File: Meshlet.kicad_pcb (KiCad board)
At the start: 4 copper layers, 42.5 x 32 mm, 101 parts, among them J12 GPS Header, J13 Thermistor Pins, J14 Ext. Notif. Header, J2 User Btn Header, J3 Batt. Header (Picoblade 1.25), J4 Batt. Header (JST-PH 2.0), J5 USB_C_Receptacle_USB2.0_16P, J6 I2C Header, J7 Ext. Power Header, J9 Ext. Power Header, Q1 AO3400A, SW2 BOOTSEL, U1 XC6206PxxxMR, U11 INA3221, U2 USBLC6-2SC6, U3 XC6206PxxxMR, U4 RP2350_60QFN, U5 Wio-SX1262, U6 BQ25185, U7 BME280, U8 W25Q32JVZP, U9 XC6206PxxxMR, Y1 12.000MHz

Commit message: Trace and zone tune-ups
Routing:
- net GND: track 3.42 -> 5.47 mm, vias 316 -> 275
- net /Pi +3V3: track 102.7 -> 103.3 mm
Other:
- board text added: "SOLAR/EXT 3.3V-18V"
- board text removed: "EXT. INPUT 3.3V-18V"

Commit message: Rounded all of the traces on the top layer. For fun
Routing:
- net /LoRa +3V3: track 49.0 -> 50.8 mm
- net USER_BTN: track 13.1 -> 14.4 mm
- net +3V3: track 89.7 -> 88.6 mm
- net Net-(U6-STAT2): track 9.58 -> 10.5 mm
- net /Pi +3V3: track 103.3 -> 104.2 mm
- net NOTIFY: track 15.8 -> 16.6 mm
- net LORA_IRQ: track 14.2 -> 14.8 mm
- net HB: track 27.8 -> 28.4 mm
- net VSET: track 9.04 -> 9.59 mm
- net GND: track 5.47 -> 5.48 mm, vias 275 -> 262

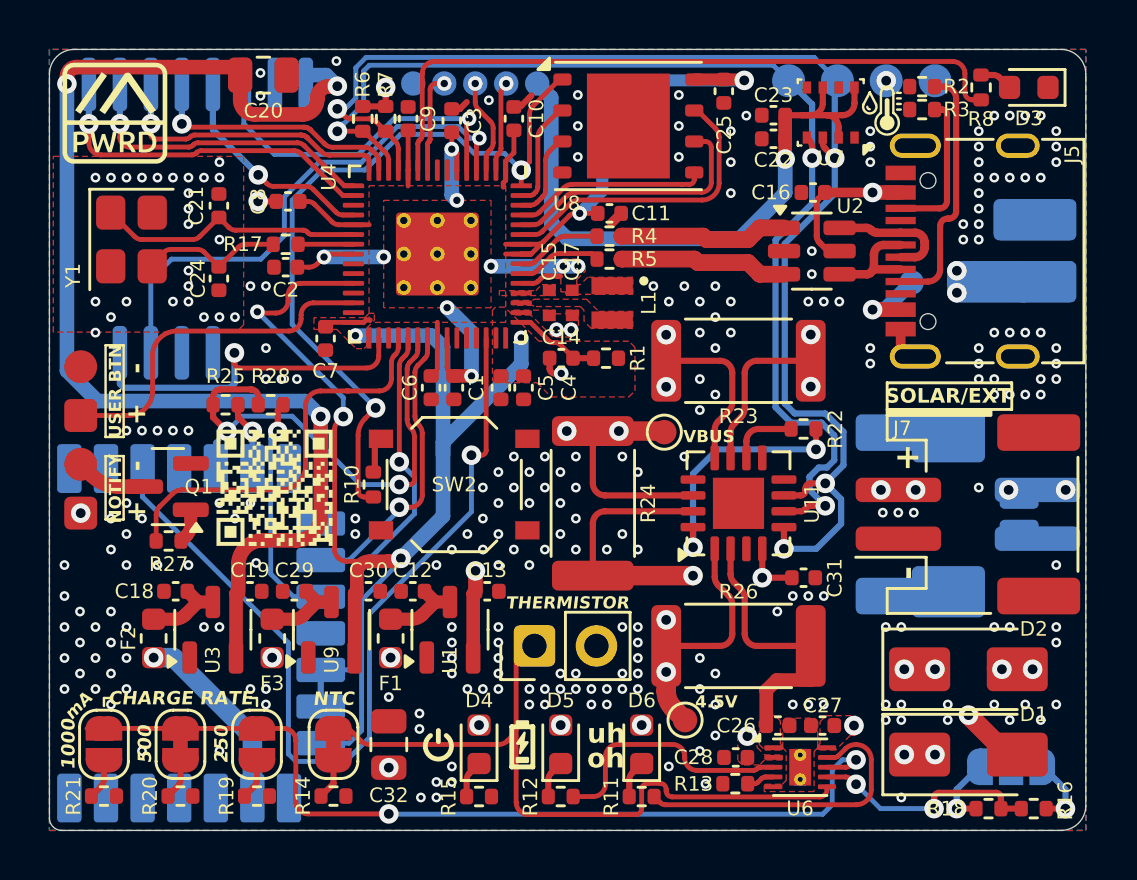
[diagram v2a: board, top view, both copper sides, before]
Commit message: Rounded traces on the back side too, updated ibom
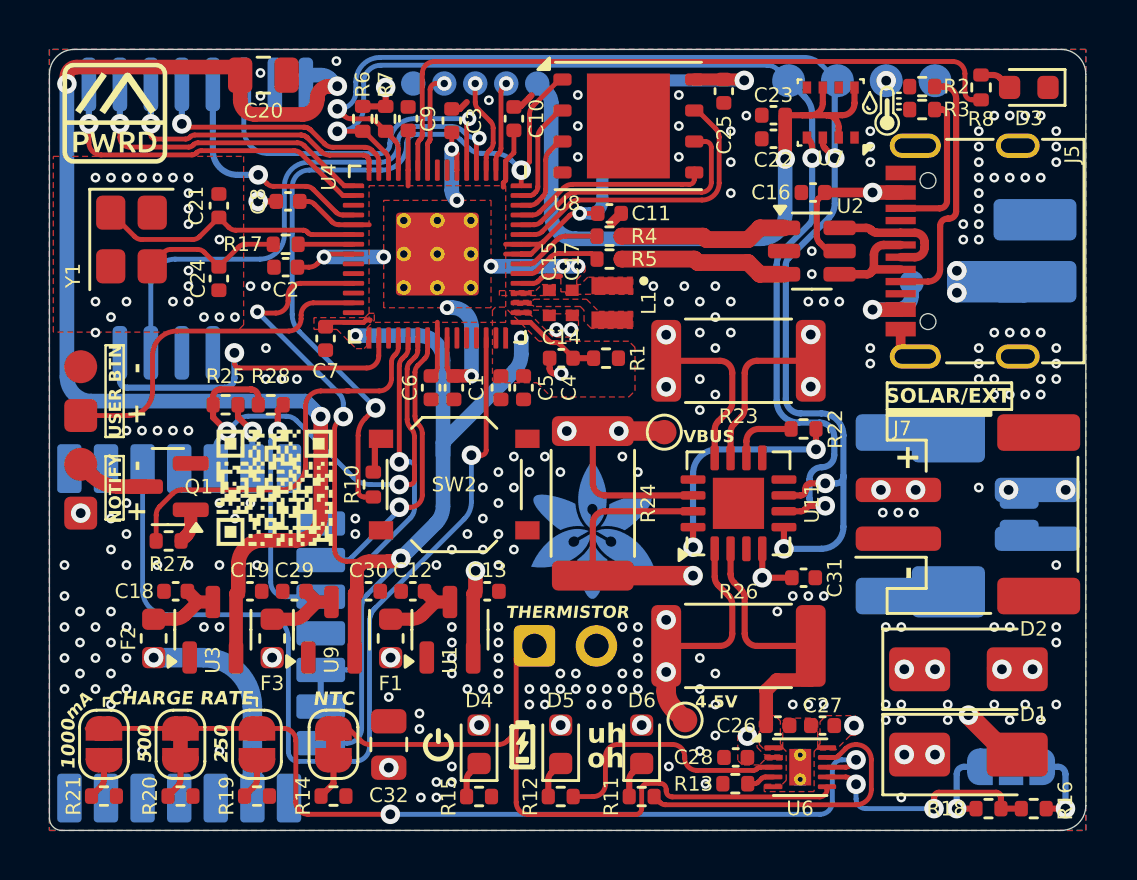
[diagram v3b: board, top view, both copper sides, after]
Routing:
- net GP29: track 36.6 -> 39.4 mm
- net BMS_OUT: track 48.0 -> 48.9 mm
- net LORA_RST: track 9.02 -> 9.64 mm
- net LORA_BUSY: track 21.5 -> 22.2 mm
- net +3V3: track 88.6 -> 89.1 mm
- net GND: vias 262 -> 242
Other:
- board text added: "by dj505"
- board text added: "designed in Edmonton, AB"
- board text added: "rev 1.0"
- board text removed: "DESIGNED IN EDMONTON, AB"

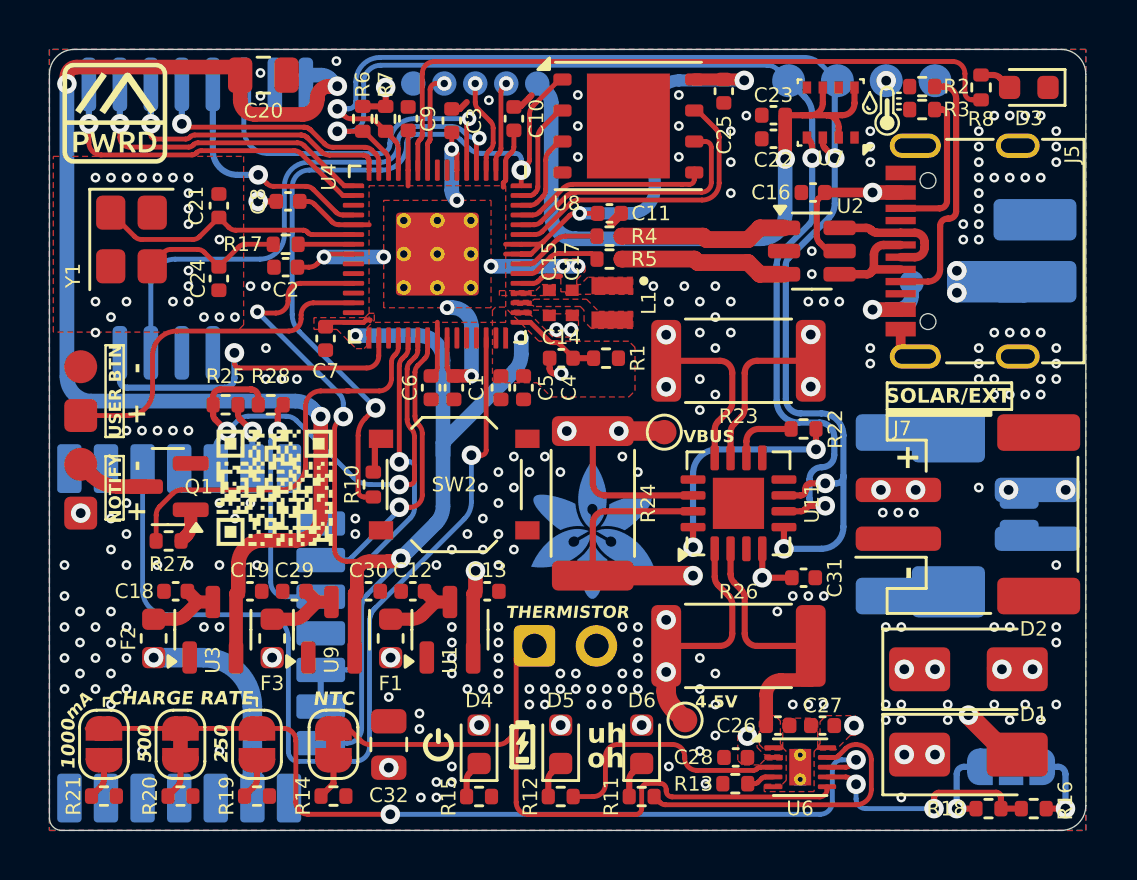
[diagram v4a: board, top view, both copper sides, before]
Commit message: Bigger vias. Less manufacturing fees. I hope
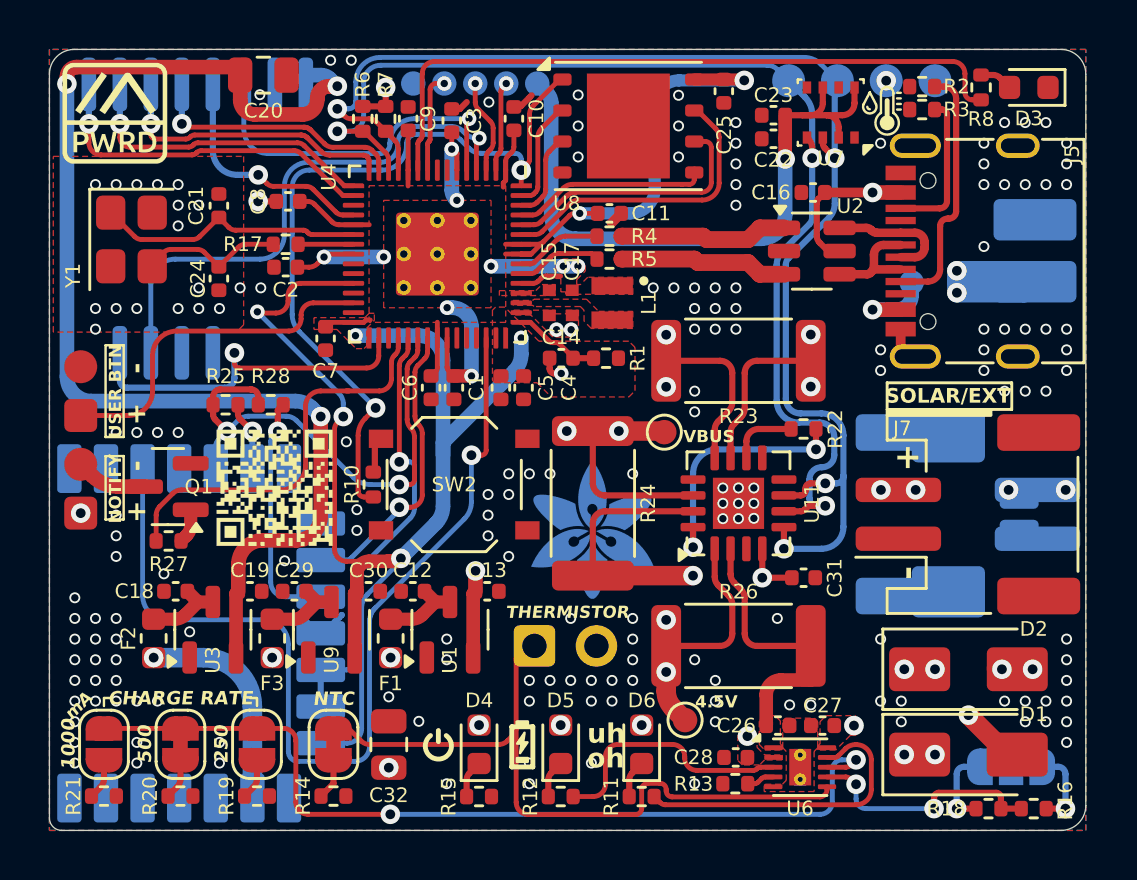
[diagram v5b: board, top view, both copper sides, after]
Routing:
- net GND: track 5.48 -> 8.08 mm, vias 242 -> 178
- net ISET: track 37.7 -> 37.0 mm

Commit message: accidentally shorted the inner layers oops
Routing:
- net +3V3: track 89.1 -> 90.3 mm
- net VBUS_OUT: track 28.8 -> 29.4 mm
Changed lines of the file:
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@@
-	(segment
-		(start 152.6289 83.028)
-		(end 151.384 84.2729)
-		(width 0.8)
-		(layer "In1.Cu")
-		(net 4)
-	)
 	(segment
 		(start 152.6289 83.028)
@@
 	)
 	(segment
-		(start 151.384 99.879799)
-		(end 151.6902 100.185999)
-		(width 0.8)
-		(layer "In1.Cu")
-		(net 4)
-	)
-	(segment
 		(start 154.0129 79.8195)
 		(end 156.7688 79.8195)
@@
 	)
 	(segment
-		(start 151.384 84.2729)
-		(end 151.384 99.879799)
+		(start 153.5303 99.5553)
+		(end 152.899601 100.185999)
+		(width 0.8)
+		(layer "In1.Cu")
+		(net 4)
+	)
+	(segment
+		(start 152.6286 83.0283)
+		(end 152.6286 97.4344)
+		(width 0.8)
+		(layer "In1.Cu")
+		(net 4)
+	)
+	(segment
+		(start 152.6289 83.028)
+		(end 152.6286 83.0283)
+		(width 0.8)
+		(layer "In1.Cu")
+		(net 4)
+	)
+	(segment
+		(start 152.6286 97.4344)
+		(end 153.5303 98.3361)
+		(width 0.8)
+		(layer "In1.Cu")
+		(net 4)
+	)
+	(segment
+		(start 152.899601 100.185999)
+		(end 151.6902 100.185999)
+		(width 0.8)
+		(layer "In1.Cu")
+		(net 4)
+	)
+	(segment
+		(start 153.5303 98.3361)
+		(end 153.5303 99.5553)
 		(width 0.8)
 		(layer "In1.Cu")
@@
 	)
 	(segment
+		(start 151.7819 95.2796)
+		(end 152.71965 96.21735)
+		(width 0.8)
+		(layer "In2.Cu")
+		(net 11)
+	)
+	(segment
 		(start 145.813 94.1755)
 		(end 149.5645 94.1755)
@@
 	(segment
 		(start 149.5645 94.1755)
+		(end 150.6686 95.2796)
+		(width 0.8)
+		(layer "In2.Cu")
+		(net 11)
+	)
+	(segment
+		(start 155.4468 100.0578)
+		(end 155.4468 106.243599)
+		(width 0.8)
+		(layer "In2.Cu")
+		(net 11)
+	)
+	(segment
+		(start 152.71965 97.33065)
 		(end 155.4468 100.0578)
 		(width 0.8)
@@
 	)
 	(segment
-		(start 155.4468 100.0578)
-		(end 155.4468 106.243599)
-		(width 0.8)
-		(layer "In2.Cu")
+		(start 150.6686 95.2796)
+		(end 151.7819 95.2796)
+		(width 0.8)
+		(layer "In2.Cu")
+		(net 11)
+	)
+	(segment
+		(start 152.71965 96.21735)
+		(end 152.71965 97.33065)
+		(width 0.8)
+		(layer "In2.Cu")
